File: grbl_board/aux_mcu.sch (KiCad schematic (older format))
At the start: 51 parts

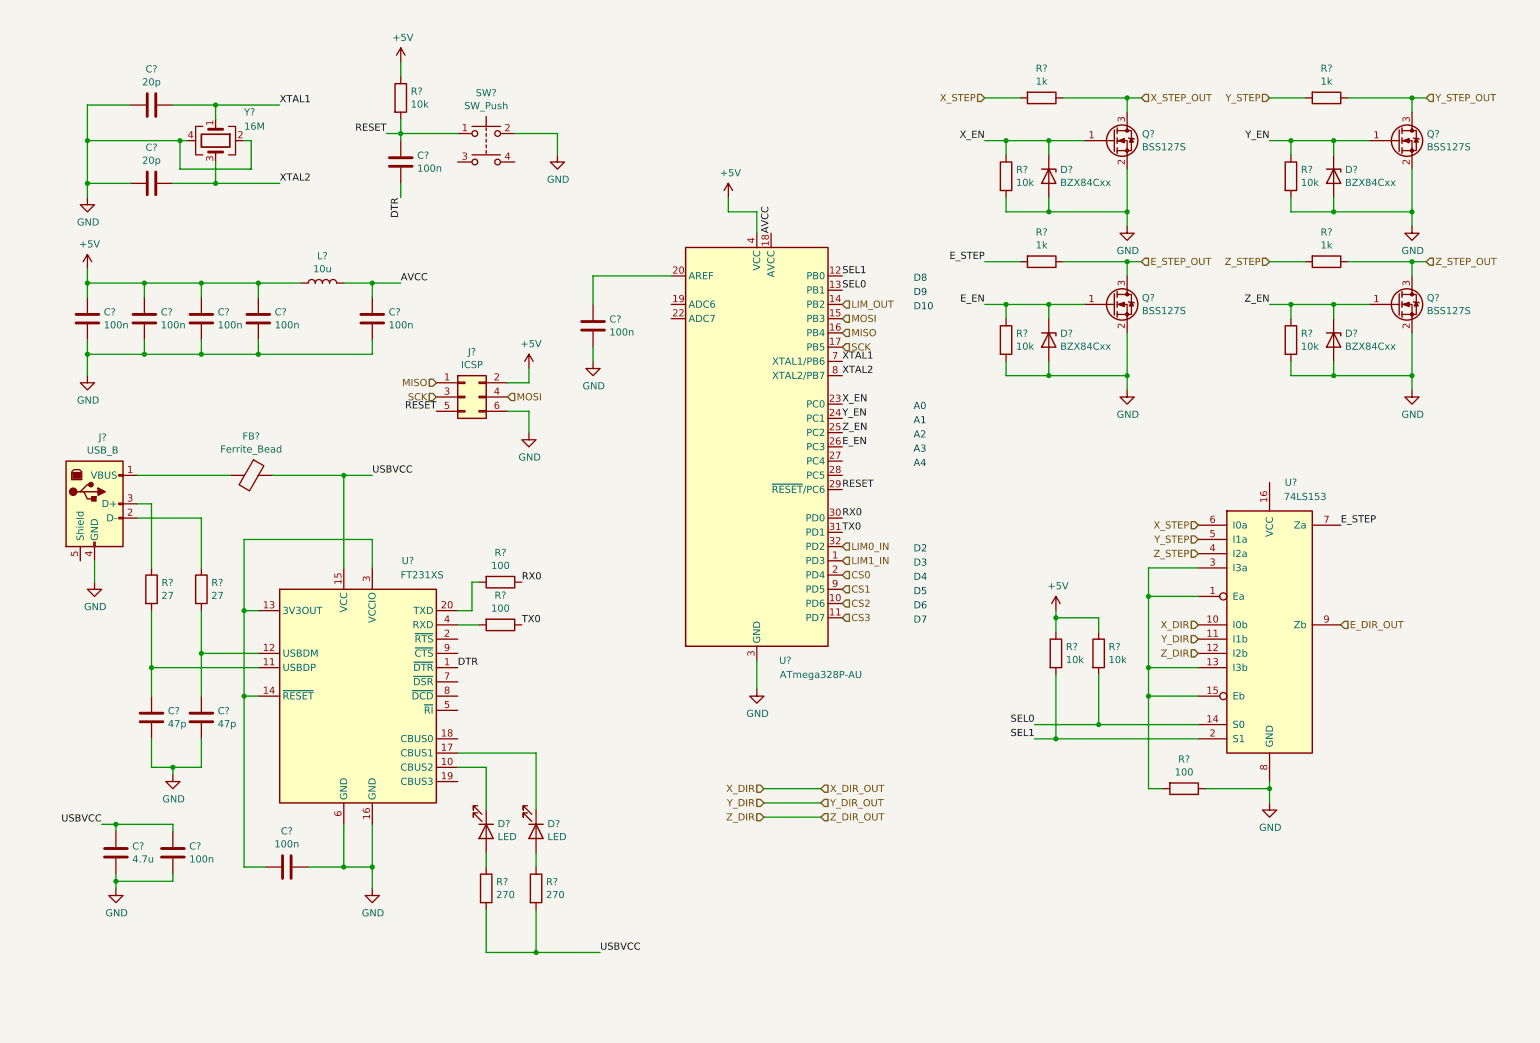
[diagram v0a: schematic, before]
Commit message: changed limit switch control
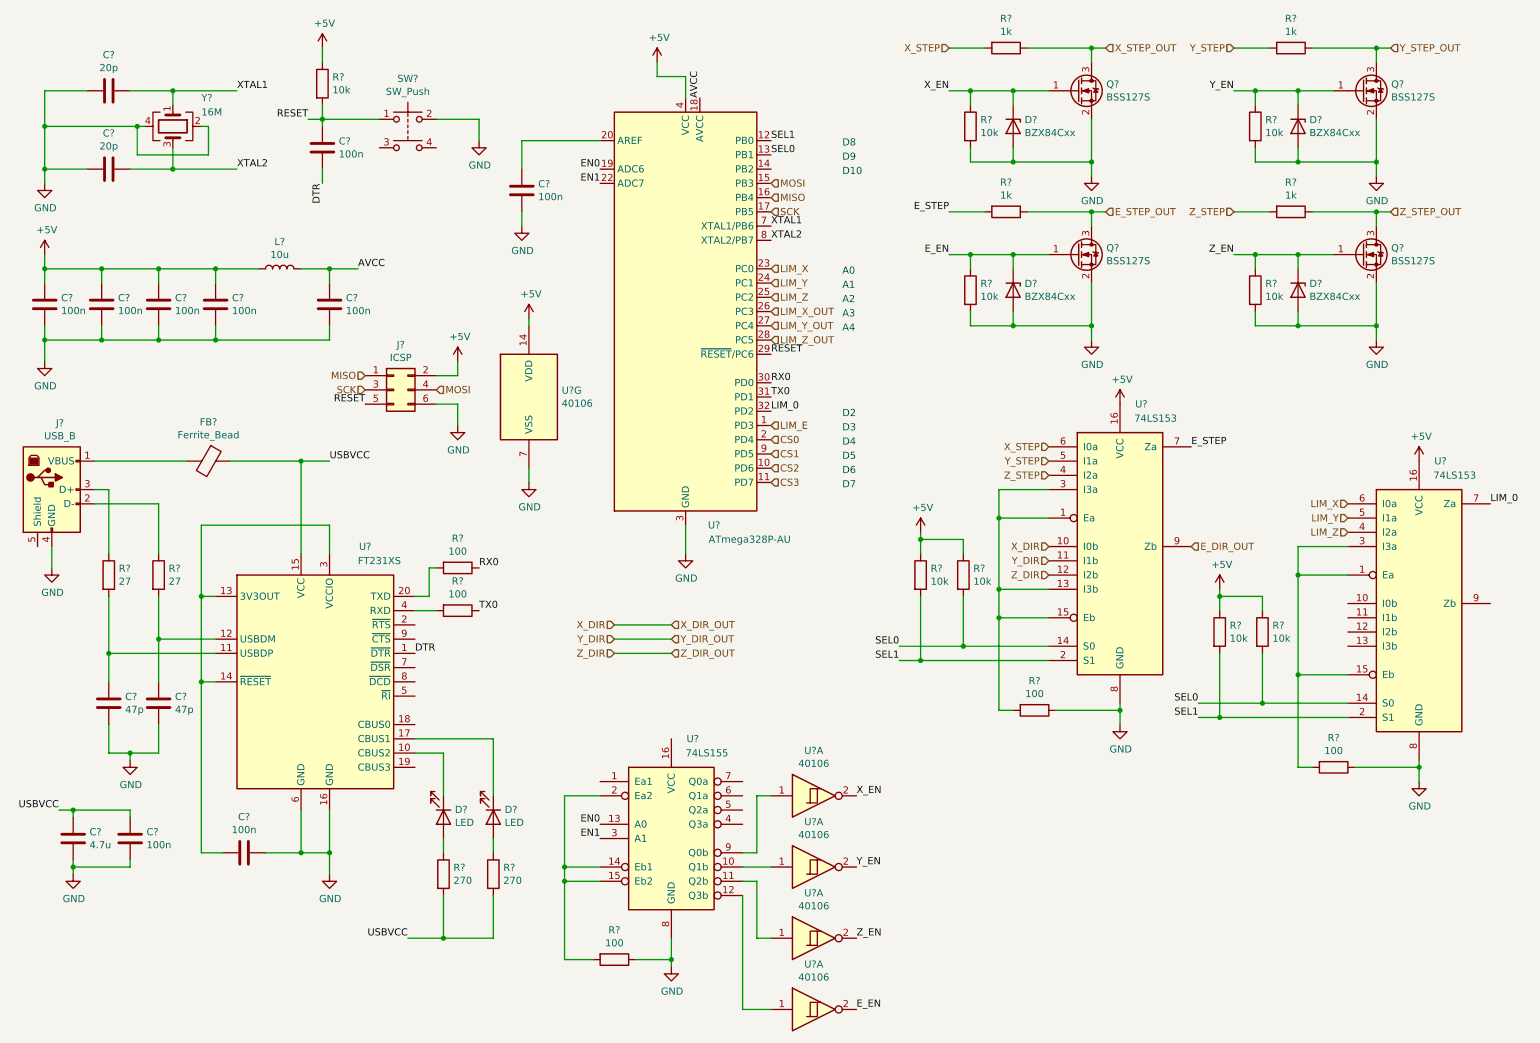
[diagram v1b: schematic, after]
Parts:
- added R? (x2): 10k, symbol Device:R
- added R? (x2): 100, symbol Device:R
- added U?: 74LS153, symbol 74xx:74LS153
- added U?: 74LS155, symbol 74xx:74LS155
- added U? (x5): 40106, symbol 4xxx:40106
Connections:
- net +5V: now also U?.16 (VCC), R?.1, R?.1, U?.14 (VDD), U?.16 (VCC)
- net E_EN: now also U?.2; no longer U?.26 (PC3)
- net GND: now also R?.1, R?.1, U?.7 (VSS), U?.8 (GND), U?.8 (GND)
- net SEL0: now also R?.2, U?.14 (S0)
- net SEL1: now also R?.2, U?.2 (S1)
- net X_EN: now also U?.2; no longer U?.23 (PC0)
- net Y_EN: now also U?.2; no longer U?.24 (PC1)
- net Z_EN: now also U?.2; no longer U?.25 (PC2)
- net EN0: now reaches U?.19 (ADC6)
- net EN0: now also U?.13 (A0)
- net EN1: now reaches U?.22 (ADC7)
- net EN1: now also U?.3 (A1)
- net LIM_Y_OUT: now reaches U?.27 (PC4)
- net LIM_Z_OUT: now reaches U?.28 (PC5)
- net LIM0_IN renamed LIM_0
- net LIM_0: now also U?.7 (Za)
- net LIM1_IN renamed LIM_E
- net LIM_OUT: no longer names the net of U?.14 (PB2)
- new net: R?.2, U?.1 (Ea), U?.15 (Eb), U?.3 (I3a)
- new net: U?.1, U?.10 (Q1b)
- new net: U?.1, U?.11 (Q2b)
- new net: U?.1, U?.12 (Q3b)
- new net: R?.2, U?.14 (Eb1), U?.15 (Eb2), U?.2 (Ea2)
- new net: U?.1, U?.9 (Q0b)
- new net LIM_X: U?.23 (PC0), U?.6 (I0a)
- new net LIM_X_OUT: U?.26 (PC3)
- new net LIM_Y: U?.24 (PC1), U?.5 (I1a)
- new net LIM_Z: U?.25 (PC2), U?.4 (I2a)
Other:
- moved on the sheet: C?, D?, FB?, J?, L?, Q?, R?, SW?, U?, Y?

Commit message: changed to matched resistor
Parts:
- J?: symbol Connector:USB_B -> grbl_board-rescue:USB_B-Connector
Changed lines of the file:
@@
 $EndComp
 $Comp
-L Connector:USB_B J?
+L grbl_board-rescue:USB_B-Connector J?
 U 1 1 61885CD9
 P 850 3900
